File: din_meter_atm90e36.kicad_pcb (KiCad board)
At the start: 2 copper layers, 32 x 31.1 mm, 77 parts, among them IC1 ATM90E36_ATM90E36, IC2 ATM90E36_ATM90E36, J1 GS3, J2 GS3, J3 GS3, J4 GS3, J5 GS3, J6 GS3, J7 Conn_01x10, J8 Conn_02x18_Row_Letter_First, Y1 Crystal_GND24, Y2 Crystal_GND24

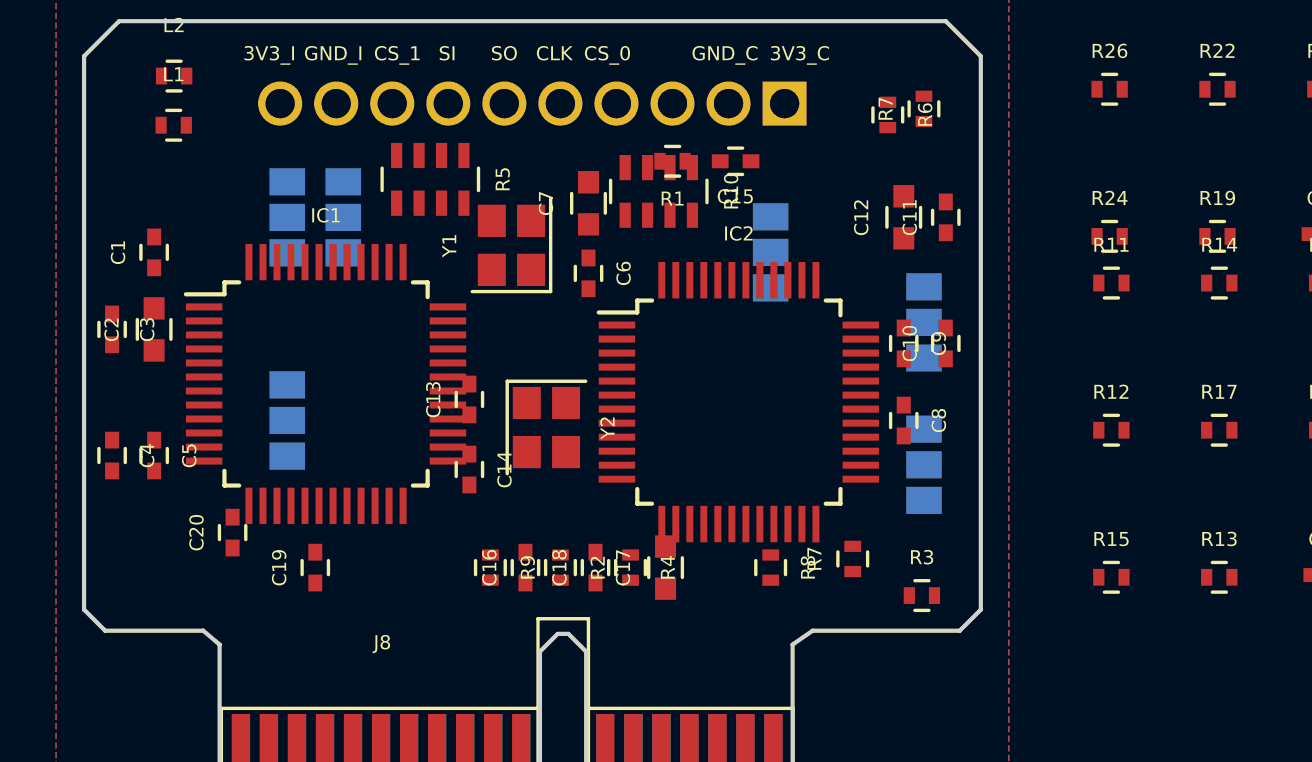
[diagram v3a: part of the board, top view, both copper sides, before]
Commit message: Change PCI-X pad names to lower case to match schema
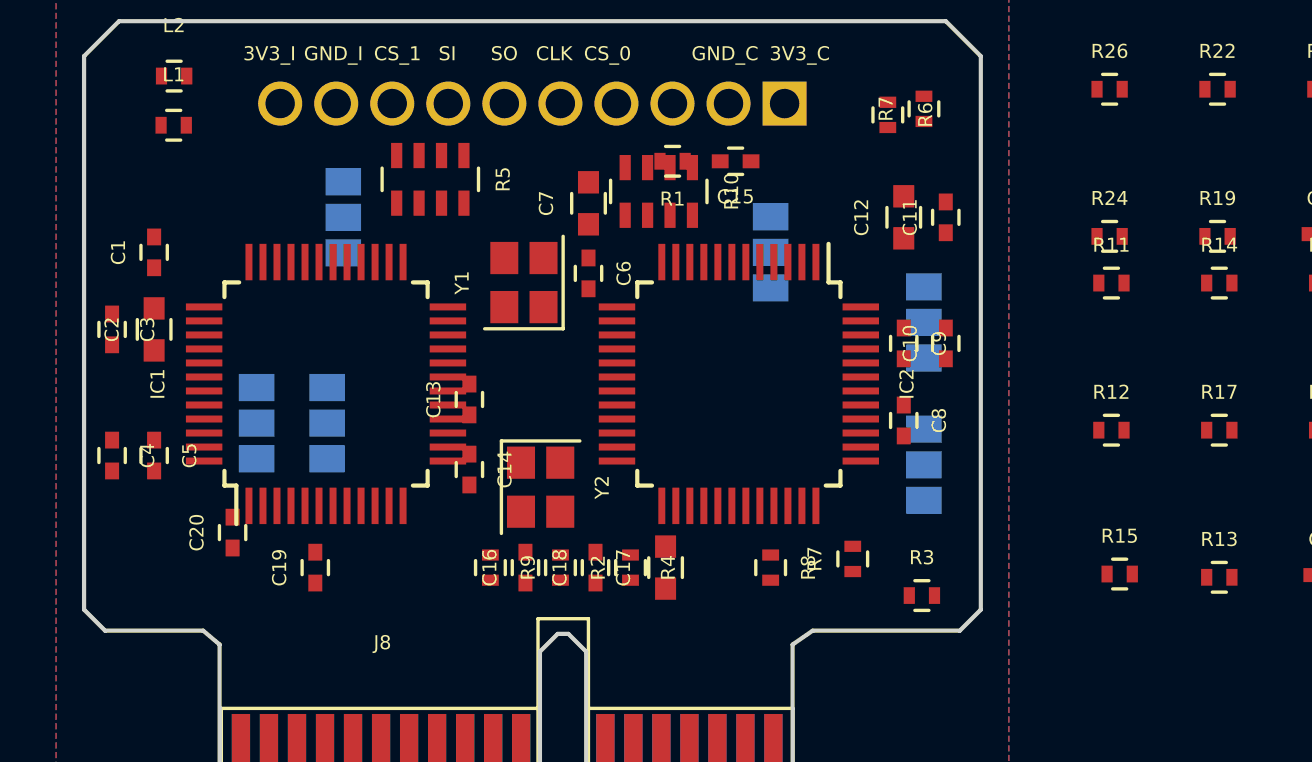
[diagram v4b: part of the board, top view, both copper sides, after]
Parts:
- C1, C11, C13, C15, C17, C18, C3, C5, C8: value C_Small -> 100n
- C10, C14, C19, C20, C4, C9: value C_Small -> 18n
- C12, C16, C2, C6: value C_Small -> 10u
- R1, R2, R4, R6, R7, R9: value R -> 1K
- R10, R5: value SMD-RES-ARRAY -> SMD-RES-ARRAY_10K
- R3: value R -> 10K
- moved J2 7.48 mm to (138.6, 72.7)
- moved Y2 2.14 mm to (146.2, 75.0)
- moved Y1 1.40 mm to (145.6, 67.7)
- moved J1 1.10 mm to (136.1, 72.7)
- moved IC2 0.65 mm to (153.3, 71.3), turned to 270 degrees
- moved R15 0.32 mm to (166.9, 78.1)
- turned IC1 to 90 degrees

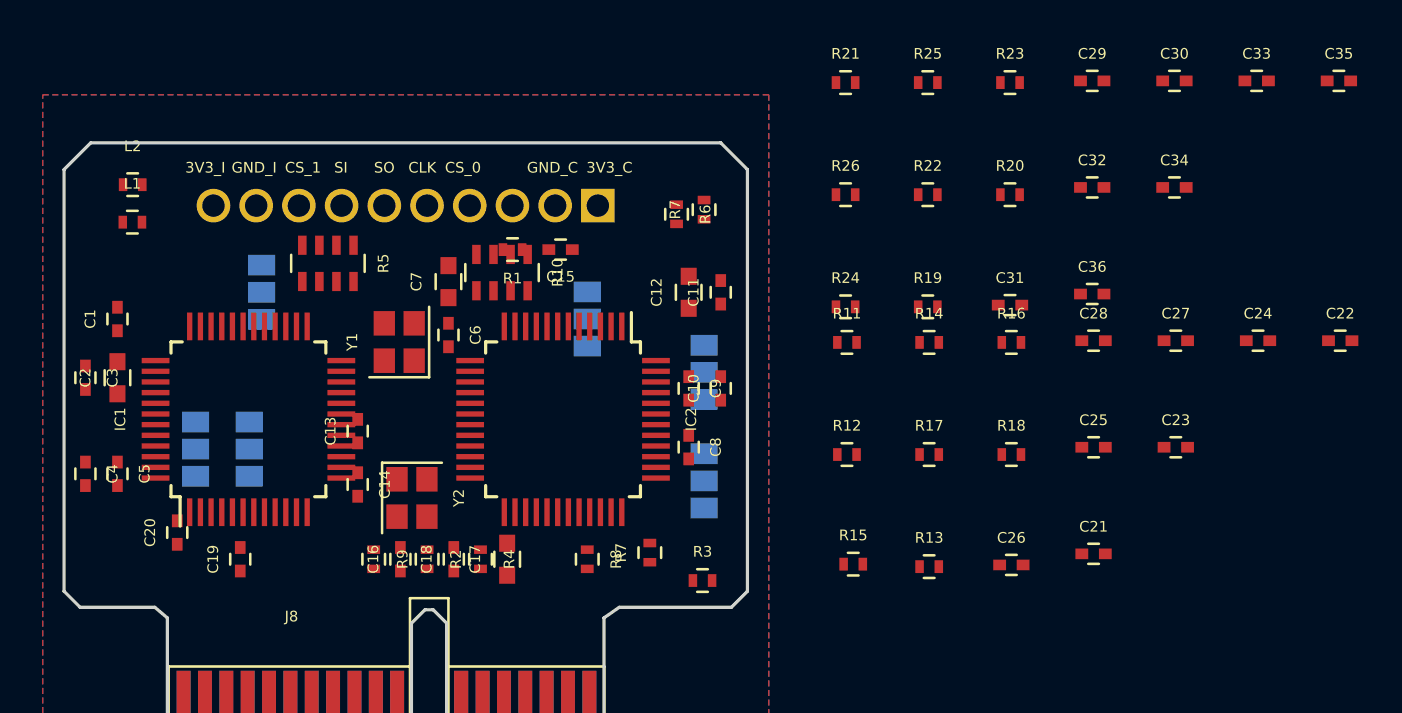
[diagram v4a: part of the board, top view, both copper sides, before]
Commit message: Change copper fill to GND
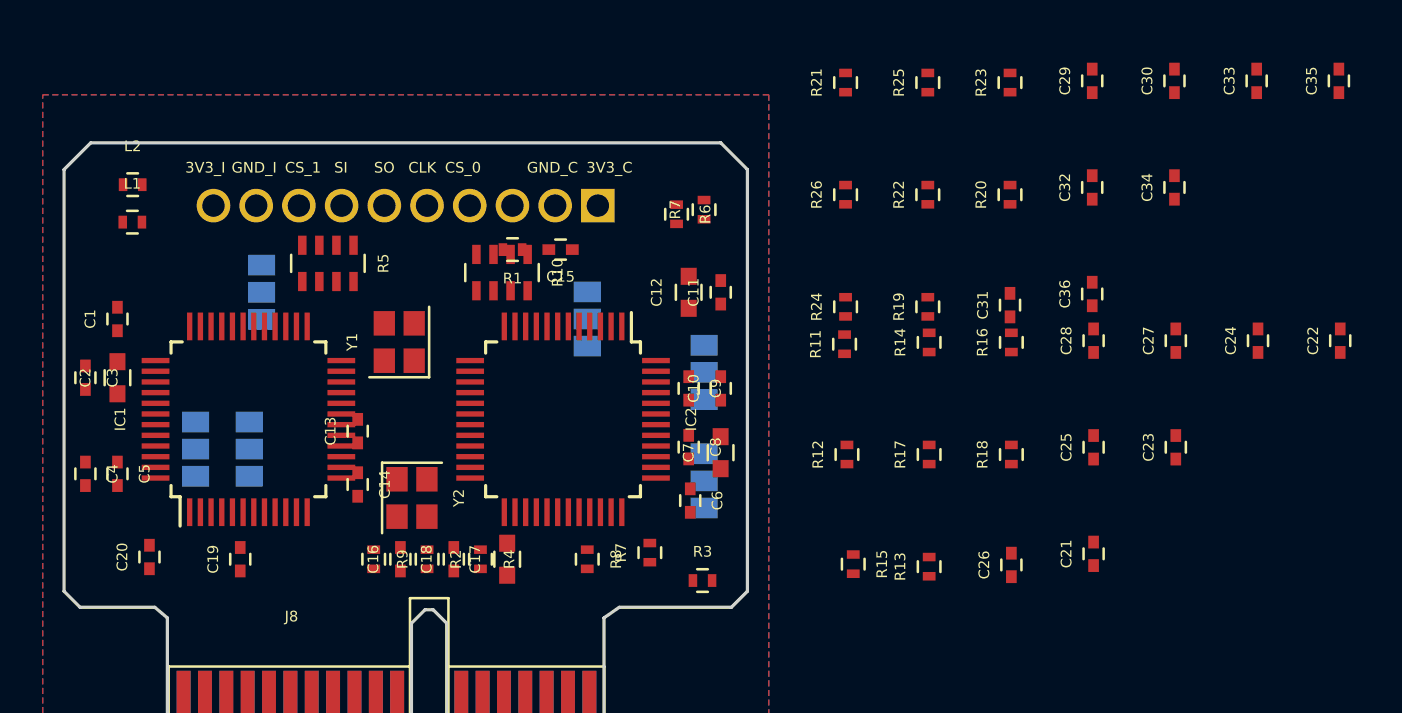
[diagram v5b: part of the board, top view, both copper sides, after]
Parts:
- moved C7 15.1 mm to (160.7, 72.9)
- moved C6 13.7 mm to (159.2, 75.2)
- moved C20 1.73 mm to (133.9, 77.8)
- moved R11 0.14 mm to (166.5, 67.8), turned to 90 degrees
- turned C21 to 90 degrees
- turned C22 to 90 degrees
- turned C23 to 90 degrees
- turned C24 to 90 degrees
- turned C25 to 90 degrees
- turned C26 to 90 degrees
- turned C27 to 90 degrees
- turned C28 to 90 degrees
- turned C29 to 90 degrees
- turned C30 to 90 degrees
- turned C31 to 90 degrees
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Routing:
- added copper zone on B.Cu, net GND
- added copper zone on F.Cu, net GND
- removed copper zone on B.Cu, net GNDD
- removed copper zone on F.Cu, net GNDD

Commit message: Clean up part placement, prep for final place and route
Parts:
- removed J1, J2, J3, J4, J5, J6: GS3, Connectors:GS3
- removed the R7 at (157.3, 77.6)
- added DMA_0: GS3, Connectors:GS3, B.Cu at (136.1, 70.8)
- added DMA_1: GS3, Connectors:GS3, B.Cu at (156.6, 70.8)
- added PM0_0: GS3, Connectors:GS3, B.Cu at (139.2, 70.8)
- added PM0_1: GS3, Connectors:GS3, B.Cu at (153.4, 70.8)
- added PM1_0: GS3, Connectors:GS3, B.Cu at (142.2, 70.8)
- added PM1_1: GS3, Connectors:GS3, B.Cu at (150.2, 70.8)
- C7: value C_Small -> 100n
- R8: value R -> 1K
- moved C33 63.2 mm to (142.6, 101.6)
- moved C29 62.7 mm to (135.7, 101.7)
- moved C30 62.7 mm to (139.5, 101.7)
- moved C22 57.3 mm to (139.5, 95.4)
- moved R23 55.2 mm to (143.8, 101.6)
- moved R6 54.6 mm to (121.7, 102.0)
- moved R20 54.5 mm to (138.3, 101.8)
- moved C34 54.3 mm to (146.5, 101.7)
- moved C35 53.8 mm to (162.0, 101.7)
- moved R7 53.2 mm to (125.2, 101.9)
- moved R19 49.0 mm to (136.9, 101.8)
- moved R21 48.5 mm to (151.3, 101.6)
- moved C24 48.2 mm to (146.6, 95.6)
- moved C32 47.7 mm to (153.9, 101.6)
- moved R25 47.3 mm to (159.3, 101.5)
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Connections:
- C16 pad 2: Net-(C16-Pad2) -> GND
- C17 pad 2: Net-(C17-Pad2) -> GND
- R10 pad 2: Net-(R10-Pad2) -> +3V3
- R10 pad 3: Net-(R10-Pad3) -> +3V3
- R10 pad 4: Net-(R10-Pad4) -> +3V3
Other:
- board text added: "Dual ATM90E36 Metering v0.1 02/01/2018"
- board text removed: "Dual ATM90E26 Metering v1.2 07/12/2017"

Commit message: Intial work from Joslyn
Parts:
- removed C13: 100n, Capacitors_SMD:C_0402
- removed C17: 100n, Capacitors_SMD:C_0603
- removed R10, R5: SMD-RES-ARRAY_10K, Resistors_SMD:R_Array_Concave_4x0603
- C16, C6: footprint Capacitors_SMD:C_0402 -> Capacitors_SMD:C_0603
- C3: value 100n -> 10u; footprint Capacitors_SMD:C_0402 -> Capacitors_SMD:C_0603
- C7: value 100n -> 10u
- moved C4 44.9 mm to (159.0, 72.5), turned to 180 degrees
- moved R1 44.1 mm to (158.9, 71.5), turned to 0 degrees
- moved C9 43.5 mm to (159.0, 69.4), turned to 180 degrees
- moved R2 41.9 mm to (158.9, 70.4), turned to 0 degrees
- moved C10 41.7 mm to (159.0, 67.3), turned to 180 degrees
- moved R4 39.9 mm to (158.9, 68.3), turned to 0 degrees
- moved R8 39.3 mm to (131.3, 64.8)
- moved C20 38.0 mm to (143.8, 67.3), turned to 180 degrees
- moved C19 38.0 mm to (143.8, 69.4), turned to 180 degrees
- moved R6 37.7 mm to (143.7, 71.5), turned to 0 degrees
- moved C14 37.6 mm to (143.8, 72.5), turned to 180 degrees
- moved C18 37.4 mm to (131.3, 66.7), turned to 270 degrees
- moved R9 36.6 mm to (143.7, 68.3), turned to 0 degrees
- moved R7 36.5 mm to (143.7, 70.4), turned to 0 degrees
- moved C16 36.1 mm to (131.2, 69.7), turned to 270 degrees
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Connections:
- C1 pad 1: +3V3 -> GND
- C1 pad 2: GND -> +3V3
- C11 pad 1: +3V3 -> GND
- C11 pad 2: GND -> +3V3
- C3 pad 2: Net-(C2-Pad2) -> +3V3
- C6 pad 2: Net-(C6-Pad2) -> GND
- C7 pad 1: Net-(C6-Pad1) -> GND
- C7 pad 2: Net-(C7-Pad2) -> +3V3
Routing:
- net GND: track 0.00 -> 21.1 mm, vias 0 -> 20
- net V2P: track 0.00 -> 14.4 mm
- net V3P: track 0.00 -> 14.0 mm
- net +3V3: track 0.00 -> 12.2 mm
- net V1P: track 0.00 -> 10.7 mm
- net Net-(IC2-Pad21): track 0.00 -> 6.58 mm
- net Net-(IC1-Pad21): track 0.00 -> 6.58 mm
- net Net-(IC2-Pad20): track 0.00 -> 4.81 mm
- net Net-(IC1-Pad20): track 0.00 -> 4.81 mm
- net Net-(C6-Pad1): track 0.00 -> 4.62 mm
- net Net-(C8-Pad1): track 0.00 -> 3.95 mm
- net Net-(C18-Pad1): track 0.00 -> 3.95 mm
- net Net-(C16-Pad1): track 0.00 -> 3.28 mm
- net Net-(C4-Pad2): track 0.00 -> 3.25 mm
- net Net-(C14-Pad2): track 0.00 -> 3.14 mm
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
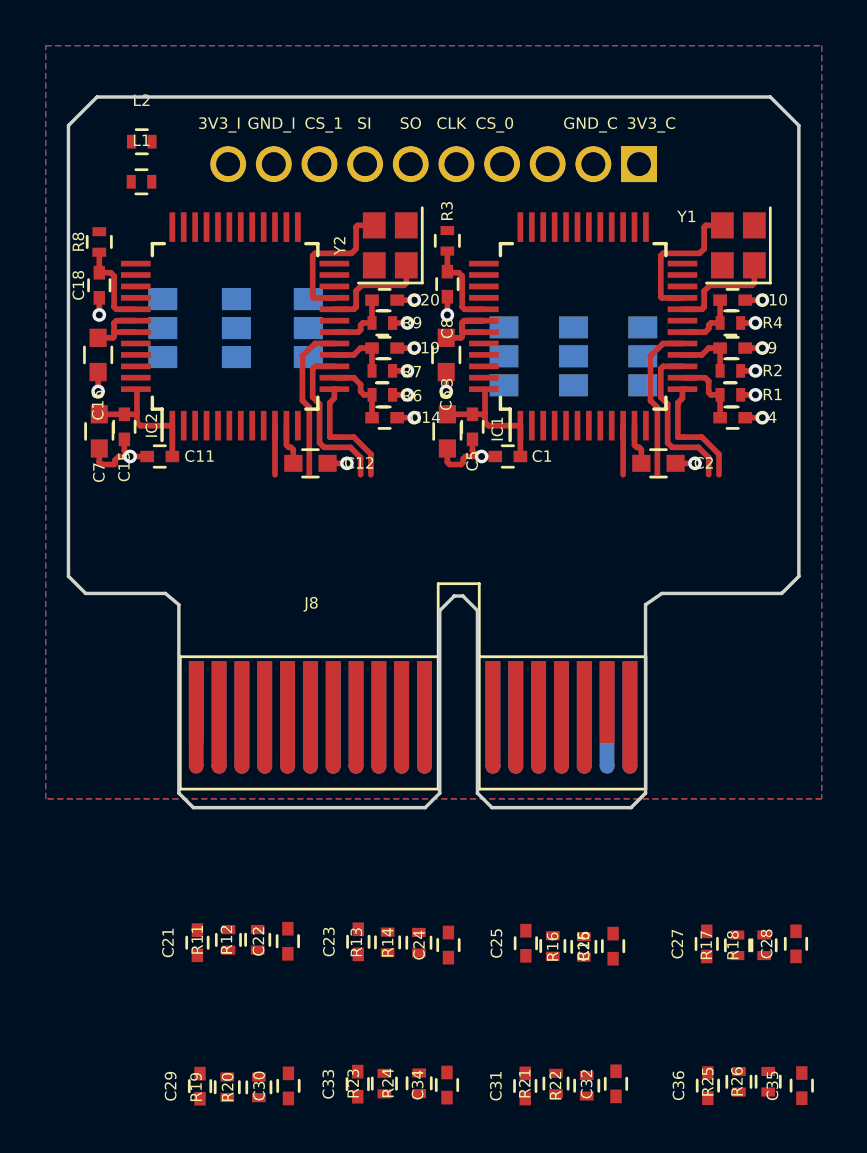
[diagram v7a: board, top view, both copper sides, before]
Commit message: Try 4-layer
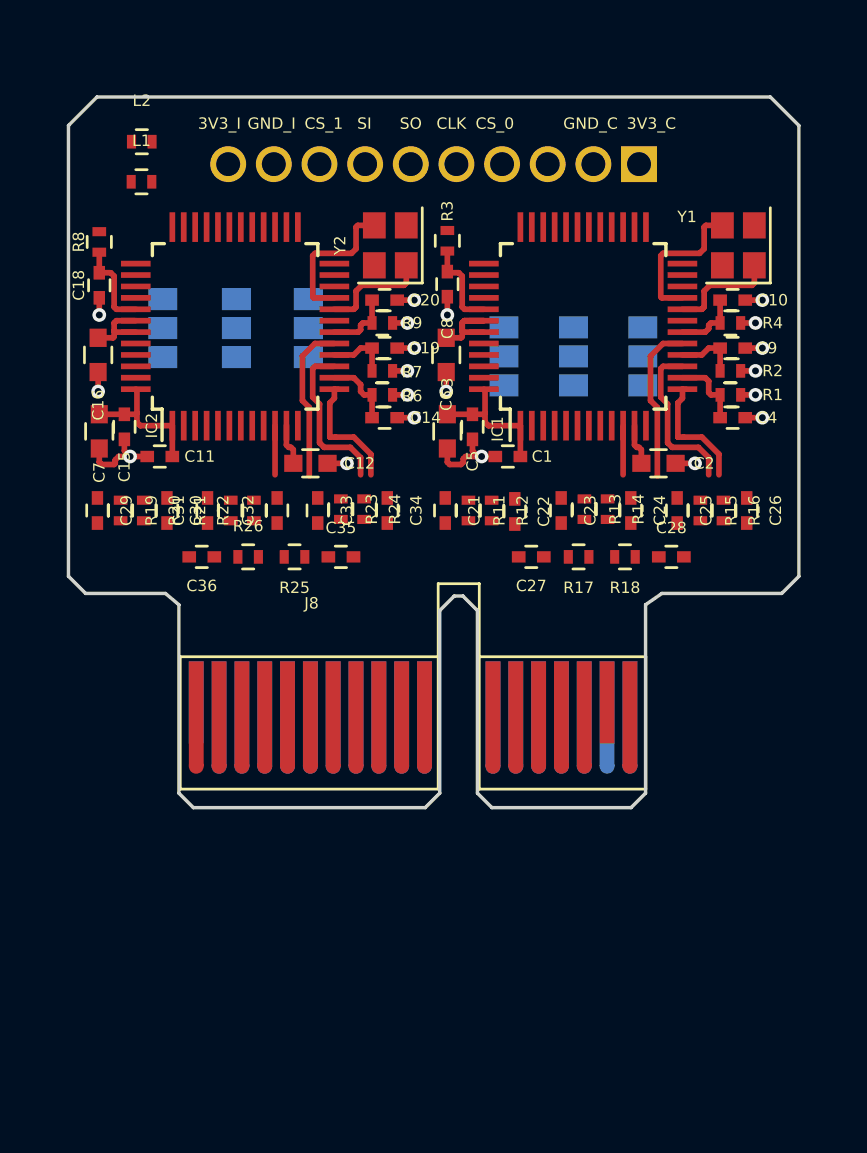
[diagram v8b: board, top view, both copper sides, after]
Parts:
- moved R26 32.4 mm to (137.8, 78.5), turned to 0 degrees
- moved C36 32.1 mm to (135.8, 78.5), turned to 180 degrees
- moved C35 30.7 mm to (141.8, 78.5), turned to 0 degrees
- moved R25 30.1 mm to (139.8, 78.5), turned to 180 degrees
- moved C32 29.2 mm to (139.1, 76.5)
- moved R22 29.1 mm to (138.0, 76.5)
- moved R21 28.9 mm to (137.0, 76.5)
- moved C31 28.8 mm to (136.0, 76.5)
- moved R20 25.8 mm to (133.2, 76.5), turned to 270 degrees
- moved C30 25.8 mm to (134.2, 76.5), turned to 270 degrees
- moved R19 25.7 mm to (132.2, 76.5), turned to 270 degrees
- moved C29 25.6 mm to (131.2, 76.5), turned to 270 degrees
- moved C34 25.3 mm to (143.9, 76.5), turned to 270 degrees
- moved R24 25.3 mm to (142.9, 76.5), turned to 270 degrees
- moved R23 25.2 mm to (141.8, 76.5), turned to 270 degrees
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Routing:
- removed copper zone on B.Cu, net GND
- removed copper zone on F.Cu, net GND
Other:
- copper layers 2 -> 4
